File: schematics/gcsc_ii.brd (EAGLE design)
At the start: 63.2 x 45.7 mm, 41 parts, among them IC1 LM2574N-2-5.0, IC2 LTV-816, IC3 PIC12C508JN, J1 MAST, J2 POWER, J3 IC3_1-4, J4 IC3_5-8, J5 EXT, Q1 NTD4906N-35G, Q2 NTD4906N-35G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

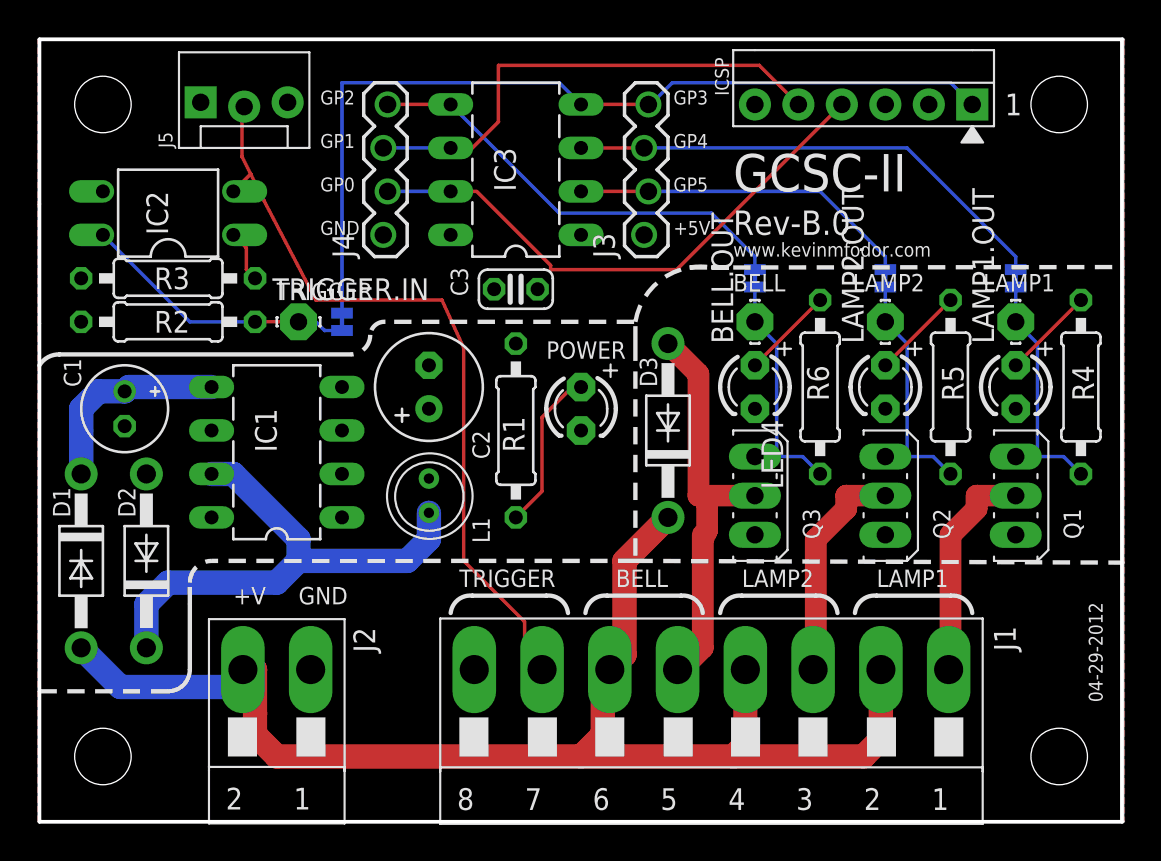
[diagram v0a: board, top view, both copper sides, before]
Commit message: Cleaned-up silk screen and some minor clean-up to traces.
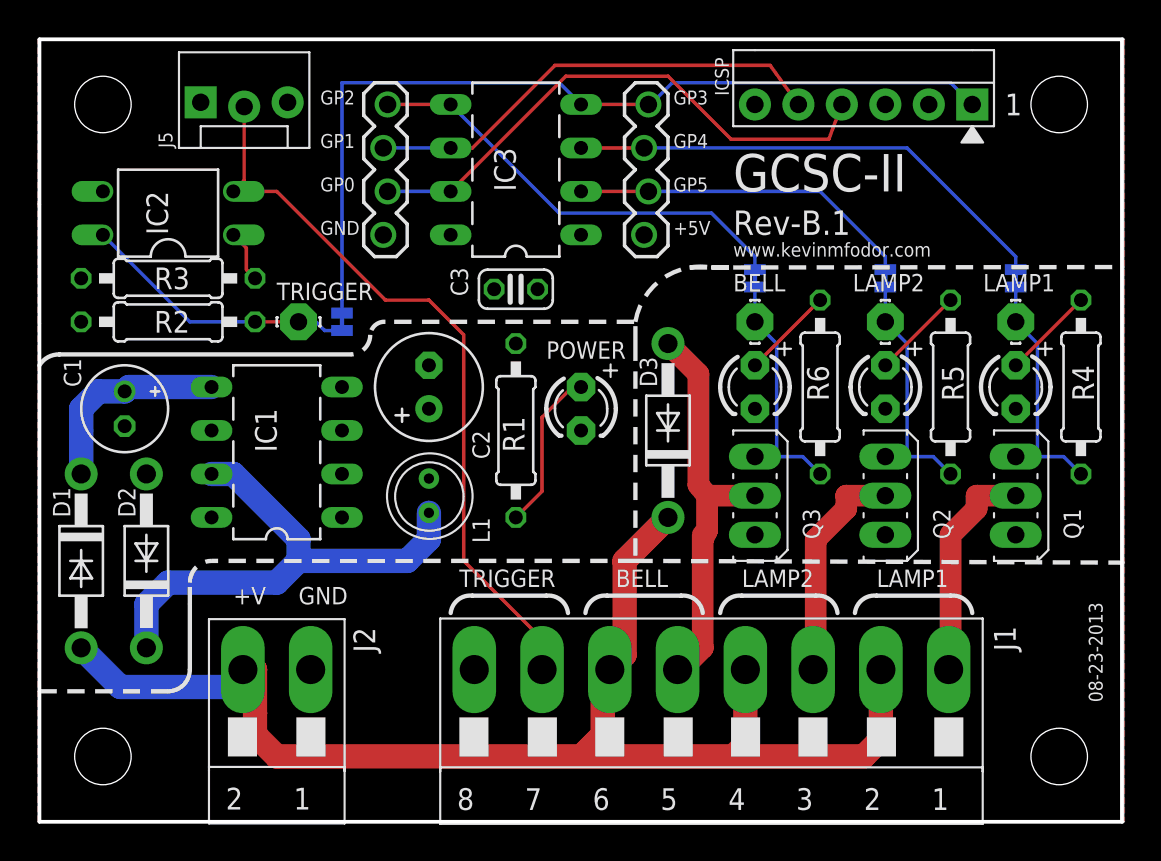
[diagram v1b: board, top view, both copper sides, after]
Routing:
- net GP1: track 29.1 -> 27.4 mm
- net TRIGGER: track 45.0 -> 43.6 mm
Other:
- board text added: "08-23-2013"
- board text added: "Rev-B.1"
- board text removed: "04-29-2012"
- board text removed: "Rev-B.0"

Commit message: Cleaned-up silkscreen, thickened traces. Electrically design is unaltered
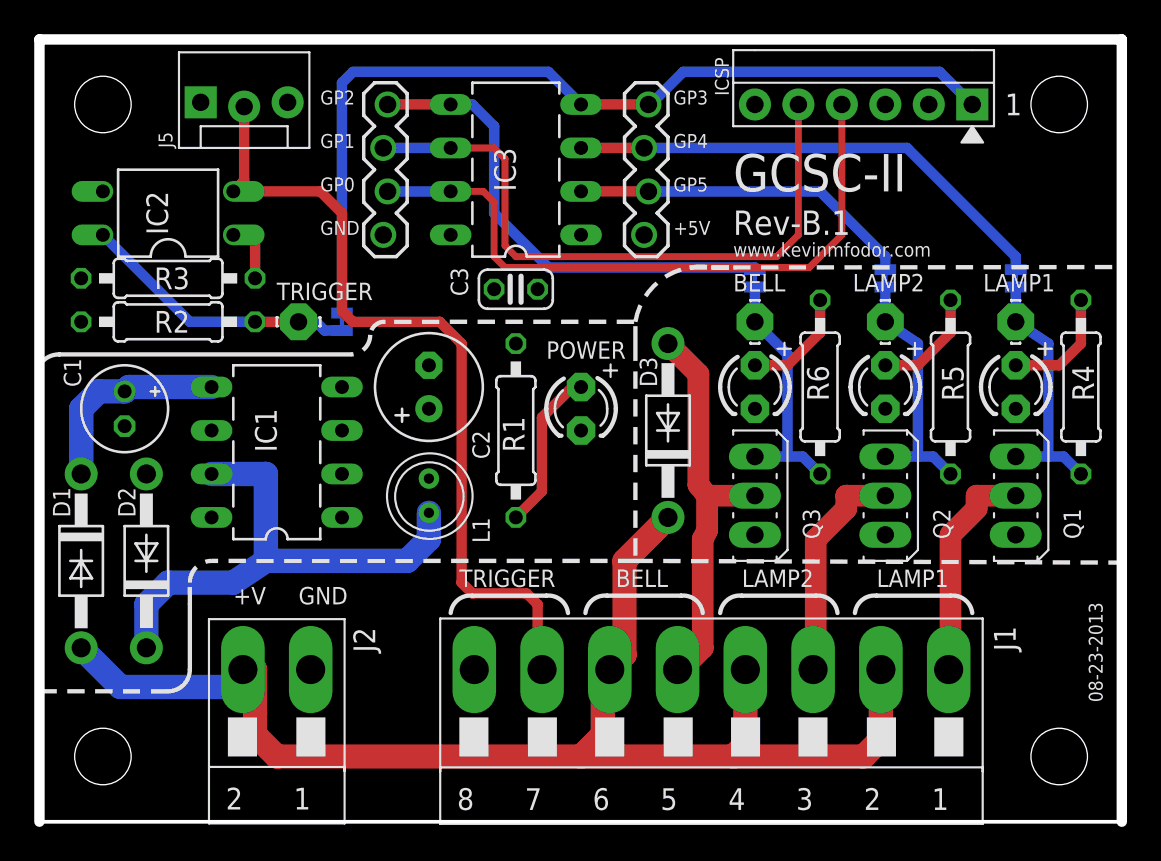
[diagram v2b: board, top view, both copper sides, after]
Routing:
- net GP1: track 27.4 -> 38.0 mm
- net GP0: track 32.3 -> 38.7 mm
- net TRIGGER: track 43.6 -> 48.4 mm
- net GP2: track 25.9 -> 28.5 mm
- net N$5: track 5.39 -> 6.88 mm
- net N$7: track 5.39 -> 6.50 mm
- net N$6: track 5.39 -> 6.50 mm
- net GP3: track 51.9 -> 52.9 mm
- net BELL.OUT: track 15.9 -> 14.9 mm
- net LAMP1.OUT: track 15.9 -> 15.2 mm
- net LAMP2.OUT: track 15.9 -> 15.2 mm
- net N$1: track 3.07 -> 3.81 mm

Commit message: Updated PCB to Rev B.1 No changes to parts or design. Only some cleaning up of traces (thickening) and cosmetic improvements
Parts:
- moved C3 0.63 mm to (27.9, 30.5)
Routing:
- net GP1: track 38.0 -> 38.5 mm
- net GP0: track 38.7 -> 39.2 mm
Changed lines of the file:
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@@
 <layers>
 <layer number="1" name="Top" color="4" fill="1" visible="yes" active="yes"/>
+<layer number="2" name="Route2" color="1" fill="3" visible="no" active="no"/>
+<layer number="3" name="Route3" color="4" fill="3" visible="no" active="no"/>
+<layer number="14" name="Route14" color="1" fill="6" visible="no" active="no"/>
+<layer number="15" name="Route15" color="4" fill="6" visible="no" active="no"/>
 <layer number="16" name="Bottom" color="1" fill="1" visible="yes" active="yes"/>
 <layer number="17" name="Pads" color="2" fill="1" visible="yes" active="yes"/>
@@
 <layer number="24" name="bOrigins" color="15" fill="1" visible="yes" active="yes"/>
 <layer number="25" name="tNames" color="7" fill="1" visible="yes" active="yes"/>
-<layer number="26" name="bNames" color="7" fill="1" visible="no" active="yes"/>
+<layer number="26" name="bNames" color="7" fill="1" visible="yes" active="yes"/>
 <layer number="27" name="tValues" color="7" fill="1" visible="no" active="yes"/>
 <layer number="28" name="bValues" color="7" fill="1" visible="no" active="yes"/>
@@
 <layer number="37" name="tTest" color="7" fill="1" visible="no" active="yes"/>
 <layer number="38" name="bTest" color="7" fill="1" visible="no" active="yes"/>
-<layer number="39" name="tKeepout" color="4" fill="11" visible="no" active="yes"/>
-<layer number="40" name="bKeepout" color="1" fill="11" visible="no" active="yes"/>
-<layer number="41" name="tRestrict" color="4" fill="10" visible="no" active="yes"/>
-<layer number="42" name="bRestrict" color="1" fill="10" visible="no" active="yes"/>
-<layer number="43" name="vRestrict" color="2" fill="10" visible="no" active="yes"/>
+<layer number="39" name="tKeepout" color="4" fill="11" visible="yes" active="yes"/>
+<layer number="40" name="bKeepout" color="1" fill="11" visible="yes" active="yes"/>
+<layer number="41" name="tRestrict" color="4" fill="10" visible="yes" active="yes"/>
+<layer number="42" name="bRestrict" color="1" fill="10" visible="yes" active="yes"/>
+<layer number="43" name="vRestrict" color="2" fill="10" visible="yes" active="yes"/>
 <layer number="44" name="Drills" color="7" fill="1" visible="no" active="yes"/>
 <layer number="45" name="Holes" color="7" fill="1" visible="yes" active="yes"/>
@@
 <layer number="49" name="Reference" color="7" fill="1" visible="no" active="yes"/>
 <layer number="50" name="dxf" color="7" fill="1" visible="no" active="no"/>
-<layer number="51" name="tDocu" color="6" fill="1" visible="yes" active="yes"/>
-<layer number="52" name="bDocu" color="7" fill="1" visible="yes" active="yes"/>
+<layer number="51" name="tDocu" color="6" fill="1" visible="no" active="yes"/>
+<layer number="52" name="bDocu" color="7" fill="1" visible="no" active="yes"/>
 <layer number="53" name="tGND_GNDA" color="7" fill="9" visible="no" active="no"/>
 <layer number="54" name="bGND_GNDA" color="1" fill="9" visible="no" active="no"/>
@@
 <layer number="110" name="fp0" color="7" fill="1" visible="no" active="yes"/>
 <layer number="111" name="LPC17xx" color="7" fill="1" visible="no" active="yes"/>
+<layer number="112" name="bGTest" color="1" fill="1" visible="no" active="no"/>
+<layer number="113" name="IDFDebug" color="7" fill="1" visible="no" active="yes"/>
+<layer number="116" name="Patch_BOT" color="9" fill="4" visible="no" active="yes"/>
 <layer number="121" name="_tsilk" color="7" fill="1" visible="no" active="yes"/>
 <layer number="122" name="_bsilk" color="7" fill="1" visible="no" active="yes"/>
@@
 <layer number="124" name="bTestmark" color="7" fill="1" visible="no" active="yes"/>
 <layer number="125" name="_tNames" color="7" fill="1" visible="no" active="yes"/>
+<layer number="126" name="_bNames" color="7" fill="1" visible="no" active="yes"/>
+<layer number="127" name="_tValues" color="7" fill="1" visible="no" active="yes"/>
+<layer number="128" name="_bValues" color="7" fill="1" visible="no" active="yes"/>
 <layer number="131" name="tAdjust" color="7" fill="1" visible="no" active="yes"/>
 <layer number="132" name="bAdjust" color="7" fill="1" visible="no" active="yes"/>
 <layer number="144" name="Drill_legend" color="7" fill="1" visible="no" active="yes"/>
+<layer number="150" name="Notes" color="7" fill="1" visible="no" active="yes"/>
 <layer number="151" name="HeatSink" color="7" fill="1" visible="no" active="yes"/>
+<layer number="152" name="_bDocu" color="7" fill="1" visible="no" active="yes"/>
 <layer number="199" name="Contour" color="7" fill="1" visible="no" active="yes"/>
 <layer number="200" name="200bmp" color="1" fill="10" visible="no" active="no"/>
@@
 <layer number="220" name="Guides" color="14" fill="1" visible="no" active="yes"/>
 <layer number="221" name="221bmp" color="22" fill="1" visible="no" active="no"/>
+<layer number="222" name="222bmp" color="23" fill="1" visible="no" active="yes"/>
 <layer number="223" name="223bmp" color="24" fill="1" visible="no" active="no"/>
 <layer number="224" name="224bmp" color="25" fill="1" visible="no" active="no"/>
+<layer number="231" name="Eagle3D_PG1" color="7" fill="1" visible="no" active="yes"/>
+<layer number="232" name="Eagle3D_PG2" color="7" fill="1" visible="no" active="yes"/>
+<layer number="233" name="Eagle3D_PG3" color="7" fill="1" visible="no" active="yes"/>
+<layer number="248" name="Housing" color="7" fill="1" visible="no" active="yes"/>
+<layer number="249" name="Edge" color="7" fill="1" visible="no" active="yes"/>
 <layer number="250" name="Descript" color="3" fill="1" visible="no" active="no"/>
 <layer number="251" name="SMDround" color="12" fill="11" visible="no" active="no"/>
@@
 <dimension x1="-1.27" y1="45.72" x2="-1.27" y2="0" x3="-10.160003125" y3="22.86" textsize="3.5" layer="51" unit="inch"/>
 <text x="29.718" y="27.051" size="1.016" layer="21">POWER</text>
-<wire x1="0.1016" y1="45.72" x2="0.1016" y2="36.0934" width="0.2032" layer="21"/>
-<wire x1="0.1016" y1="36.0934" x2="0.1016" y2="29.1084" width="0.2032" layer="21"/>
-<wire x1="0.1016" y1="29.1084" x2="0.1016" y2="26.67" width="0.2032" layer="21"/>
+<wire x1="0.1016" y1="45.72" x2="0.1016" y2="26.67" width="0.2032" layer="21"/>
 <wire x1="0.1016" y1="26.67" x2="0.1016" y2="7.62" width="0.2032" layer="21"/>
 <wire x1="0.1016" y1="7.62" x2="0.1016" y2="0" width="0.2032" layer="21"/>
@@
 <text x="15.24" y="12.7" size="1.016" layer="21">GND</text>
 <text x="11.43" y="12.7" size="1.016" layer="21">+V</text>
-<wire x1="34.925" y1="27.94" x2="34.925" y2="29.21" width="0.254" layer="21" style="dashdot"/>
 <wire x1="38.1" y1="32.385" x2="39.37" y2="32.385" width="0.254" layer="21" style="dashdot"/>
-<wire x1="39.37" y1="32.385" x2="40.64" y2="32.385" width="0.254" layer="21" style="dashdot"/>
 <wire x1="40.64" y1="32.385" x2="63.3984" y2="32.4104" width="0.254" layer="21" style="dashdot"/>
-<wire x1="34.925" y1="27.94" x2="34.925" y2="15.24" width="0.254" layer="21" style="dashdot"/>
+<wire x1="34.925" y1="29.21" x2="34.925" y2="15.24" width="0.254" layer="21" style="dashdot"/>
 <wire x1="34.925" y1="15.24" x2="63.3984" y2="15.1384" width="0.254" layer="21" style="dashdot"/>
 <wire x1="20.828" y1="29.21" x2="34.925" y2="29.21" width="0.254" layer="21" style="dashdot"/>
@@
 <attribute name="PARTNO" value="EEU-FR1C221" x="22.86" y="25.4" size="1.778" layer="27" rot="R90" display="off"/>
 </element>
-<element name="C3" library="kevin" package="C025-024X044" value="0.1uF" x="27.94" y="31.115" smashed="yes" rot="R180">
-<attribute name="NAME" x="24.13" y="32.385" size="1.016" layer="21" rot="R270"/>
-<attribute name="VALUE" x="27.178" y="31.242" size="1.27" layer="27" rot="R180"/>
-<attribute name="PARTNO" value="21RZ310-RC" x="27.94" y="31.115" size="1.778" layer="27" rot="R180" display="off"/>
+<element name="C3" library="kevin" package="C025-024X044" value="0.1uF" x="27.94" y="30.48" smashed="yes" rot="R180">
+<attribute name="NAME" x="24.13" y="31.75" size="1.016" layer="21" rot="R270"/>
+<attribute name="VALUE" x="27.178" y="30.607" size="1.27" layer="27" rot="R180"/>
+<attribute name="PARTNO" value="21RZ310-RC" x="27.94" y="30.48" size="1.778" layer="27" rot="R180" display="off"/>
 </element>
 <element name="R4" library="kevin" package="0207/10" value="1k" x="60.96" y="25.4" smashed="yes" rot="R270">
@@
 <contactref element="ICSP" pad="4"/>
 <wire x1="20.447" y1="36.83" x2="24.13" y2="36.83" width="0.6096" layer="16"/>
-<wire x1="26.67" y1="33.02" x2="27.305" y2="32.385" width="0.4064" layer="1"/>
-<wire x1="27.305" y1="32.385" x2="45.085" y2="32.385" width="0.4064" layer="1"/>
-<wire x1="45.085" y1="32.385" x2="46.99" y2="34.29" width="0.4064" layer="1"/>
+<wire x1="26.67" y1="33.02" x2="27.94" y2="31.75" width="0.4064" layer="1"/>
+<wire x1="27.94" y1="31.75" x2="44.45" y2="31.75" width="0.4064" layer="1"/>
+<wire x1="44.45" y1="31.75" x2="46.99" y2="34.29" width="0.4064" layer="1"/>
 <wire x1="46.99" y1="34.29" x2="46.99" y2="41.91" width="0.4064" layer="1"/>
 <wire x1="26.67" y1="33.02" x2="26.67" y2="36.195" width="0.4064" layer="1"/>
@@
 <contactref element="ICSP" pad="5"/>
 <wire x1="20.193" y1="39.37" x2="24.13" y2="39.37" width="0.6096" layer="16"/>
-<wire x1="43.18" y1="33.02" x2="44.45" y2="34.29" width="0.4064" layer="1"/>
+<wire x1="42.545" y1="32.385" x2="44.45" y2="34.29" width="0.4064" layer="1"/>
 <wire x1="44.45" y1="34.29" x2="44.45" y2="41.91" width="0.4064" layer="1"/>
-<wire x1="43.18" y1="33.02" x2="27.94" y2="33.02" width="0.4064" layer="1"/>
-<wire x1="27.94" y1="33.02" x2="27.305" y2="33.655" width="0.4064" layer="1"/>
+<wire x1="42.545" y1="32.385" x2="28.575" y2="32.385" width="0.4064" layer="1"/>
+<wire x1="28.575" y1="32.385" x2="27.305" y2="33.655" width="0.4064" layer="1"/>
 <wire x1="27.305" y1="33.655" x2="27.305" y2="38.735" width="0.4064" layer="1"/>
 <wire x1="27.305" y1="38.735" x2="26.67" y2="39.37" width="0.4064" layer="1"/>

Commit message: Made slight modification to the top-silk to add heavier font for the "+" markings on the LEDs. Also updated to Eagle 6.6.0. Regenerated gerbers, schematic and archive.
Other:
- board text added: "+"
- board text added: "05-01-2015"
- board text added: "Rev-B.2"
- board text removed: "08-23-2013"
- board text removed: "Rev-B.1"
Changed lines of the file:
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@@
 <?xml version="1.0" encoding="utf-8"?>
 <!DOCTYPE eagle SYSTEM "eagle.dtd">
-<eagle version="6.5.0">
+<eagle version="6.6.0">
 <drawing>
 <settings>
@@
 <layer number="24" name="bOrigins" color="15" fill="1" visible="yes" active="yes"/>
 <layer number="25" name="tNames" color="7" fill="1" visible="yes" active="yes"/>
-<layer number="26" name="bNames" color="7" fill="1" visible="yes" active="yes"/>
+<layer number="26" name="bNames" color="7" fill="1" visible="no" active="yes"/>
 <layer number="27" name="tValues" color="7" fill="1" visible="no" active="yes"/>
 <layer number="28" name="bValues" color="7" fill="1" visible="no" active="yes"/>
@@
 <layer number="37" name="tTest" color="7" fill="1" visible="no" active="yes"/>
 <layer number="38" name="bTest" color="7" fill="1" visible="no" active="yes"/>
-<layer number="39" name="tKeepout" color="4" fill="11" visible="yes" active="yes"/>
-<layer number="40" name="bKeepout" color="1" fill="11" visible="yes" active="yes"/>
-<layer number="41" name="tRestrict" color="4" fill="10" visible="yes" active="yes"/>
-<layer number="42" name="bRestrict" color="1" fill="10" visible="yes" active="yes"/>
-<layer number="43" name="vRestrict" color="2" fill="10" visible="yes" active="yes"/>
+<layer number="39" name="tKeepout" color="4" fill="11" visible="no" active="yes"/>
+<layer number="40" name="bKeepout" color="1" fill="11" visible="no" active="yes"/>
+<layer number="41" name="tRestrict" color="4" fill="10" visible="no" active="yes"/>
+<layer number="42" name="bRestrict" color="1" fill="10" visible="no" active="yes"/>
+<layer number="43" name="vRestrict" color="2" fill="10" visible="no" active="yes"/>
 <layer number="44" name="Drills" color="7" fill="1" visible="no" active="yes"/>
 <layer number="45" name="Holes" color="7" fill="1" visible="yes" active="yes"/>
@@
 <layer number="49" name="Reference" color="7" fill="1" visible="no" active="yes"/>
 <layer number="50" name="dxf" color="7" fill="1" visible="no" active="no"/>
-<layer number="51" name="tDocu" color="6" fill="1" visible="no" active="yes"/>
-<layer number="52" name="bDocu" color="7" fill="1" visible="no" active="yes"/>
+<layer number="51" name="tDocu" color="6" fill="1" visible="yes" active="yes"/>
+<layer number="52" name="bDocu" color="7" fill="1" visible="yes" active="yes"/>
 <layer number="53" name="tGND_GNDA" color="7" fill="9" visible="no" active="no"/>
 <layer number="54" name="bGND_GNDA" color="1" fill="9" visible="no" active="no"/>
@@
 <circle x="3.81" y="41.91" radius="2.83980625" width="0.6096" layer="42"/>
 <circle x="3.81" y="41.91" radius="2.83980625" width="0.6096" layer="41"/>
-<text x="40.64" y="34.29" size="1.4224" layer="21" ratio="10">Rev-B.1</text>
+<text x="40.64" y="34.29" size="1.4224" layer="21" ratio="10">Rev-B.2</text>
 <dimension x1="-1.27" y1="45.72" x2="-1.27" y2="0" x3="-10.160003125" y3="22.86" textsize="3.5" layer="51" unit="inch"/>
 <text x="29.718" y="27.051" size="1.016" layer="21">POWER</text>
@@
 <rectangle x1="34.29" y1="17.653" x2="35.306" y2="27.813" layer="41"/>
 <rectangle x1="34.29" y1="19.05" x2="38.735" y2="26.67" layer="42"/>
-<text x="62.23" y="6.985" size="0.8128" layer="21" font="vector" ratio="10" rot="SR90">08-23-2013</text>
+<text x="62.23" y="6.985" size="0.8128" layer="21" font="vector" ratio="10" rot="SR90">05-01-2015</text>
 <text x="7.874" y="39.37" size="0.8128" layer="21" rot="R90">J5</text>
+<text x="29.21" y="25.4" size="1.778" layer="21" ratio="15">+</text>
+<text x="39.37" y="26.67" size="1.778" layer="21" ratio="15">+</text>
+<text x="46.99" y="26.67" size="1.778" layer="21" ratio="15">+</text>
+<text x="54.61" y="26.67" size="1.778" layer="21" ratio="15">+</text>
+<wire x1="43.815" y1="21.59" x2="43.815" y2="16.51" width="0.3048" layer="21"/>
+<wire x1="51.435" y1="21.59" x2="51.435" y2="16.51" width="0.3048" layer="21"/>
+<wire x1="59.055" y1="21.59" x2="59.055" y2="16.51" width="0.3048" layer="21"/>
 </plain>
 <attributes>
